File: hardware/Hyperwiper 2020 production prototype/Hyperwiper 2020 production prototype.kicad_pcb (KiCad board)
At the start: 2 copper layers, 79.5 x 57.3 mm, 20 parts, among them J1 Conn_01x05, K1 Main Power relay, K2 Wiper control relay, Q1 PN2222A, SW1 ON-OFF, SW2 SW_Reed, U1 Teensy4.0, U3 L7805

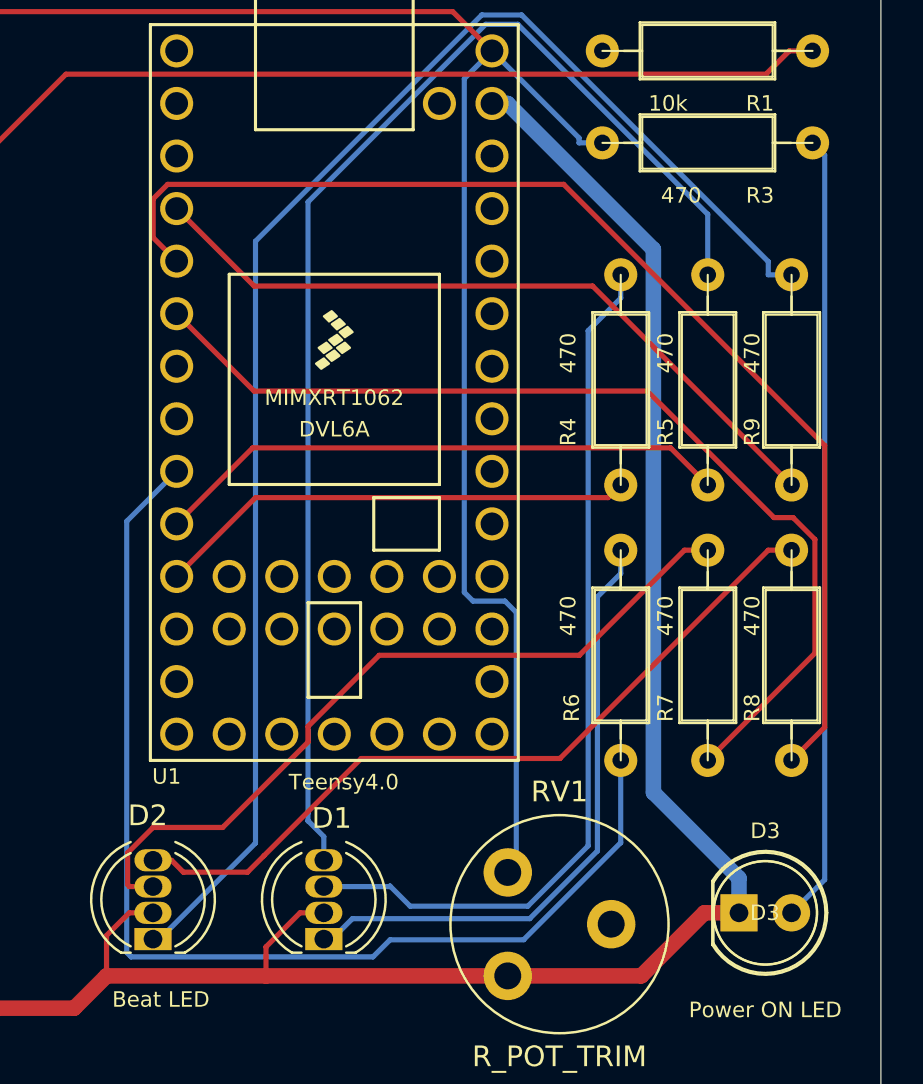
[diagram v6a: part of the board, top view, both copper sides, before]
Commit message: Added flowchart drafts and modified pin number after finding conflics with the audio board I2C bus
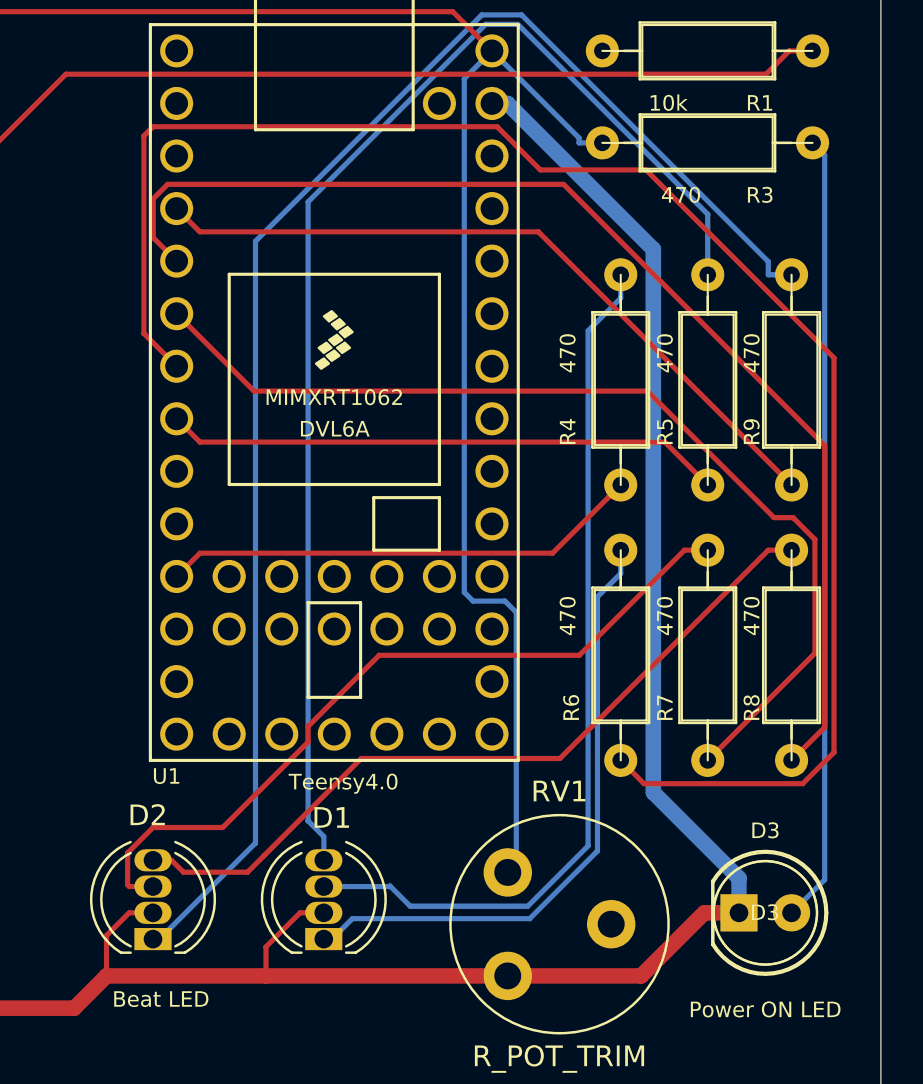
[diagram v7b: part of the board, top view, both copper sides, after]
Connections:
- U1 pad 10: /M_LED_g -> Net-(U1-Pad10)
- U1 pad 7: Net-(U1-Pad7) -> /M_LED_r
- U1 pad 8: Net-(U1-Pad8) -> /M_LED_g
- U1 pad 9: /M_LED_r -> Net-(U1-Pad9)
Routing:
- net /M_LED_r: track 54.5 -> 80.4 mm
- net /M_LED_g: track 27.9 -> 27.0 mm
- net /M_LED_b: track 23.3 -> 24.2 mm
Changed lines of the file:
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@@
   (net 26 "Net-(U1-Pad2)")
   (net 27 "Net-(U1-Pad3)")
-  (net 28 "Net-(U1-Pad7)")
-  (net 29 "Net-(U1-Pad8)")
+  (net 28 "Net-(U1-Pad9)")
+  (net 29 "Net-(U1-Pad10)")
   (net 30 "Net-(U1-Pad12)")
   (net 31 "Net-(U1-Pad13)")
@@
       (net 21 "/B_LED_b") (pinfunction "4_BCLK2"))
     (pad "7" thru_hole circle (at -1.27 7.62 270) (size 1.6 1.6) (drill 1.1) (layers *.Cu *.Mask)
-      (net 28 "Net-(U1-Pad7)") (pinfunction "5_IN2"))
+      (net 20 "/M_LED_r") (pinfunction "5_IN2"))
     (pad "8" thru_hole circle (at 1.27 7.62 270) (size 1.6 1.6) (drill 1.1) (layers *.Cu *.Mask)
-      (net 29 "Net-(U1-Pad8)") (pinfunction "6_OUT1D"))
+      (net 19 "/M_LED_g") (pinfunction "6_OUT1D"))
     (pad "9" thru_hole circle (at 3.81 7.62 270) (size 1.6 1.6) (drill 1.1) (layers *.Cu *.Mask)
-      (net 20 "/M_LED_r") (pinfunction "7_RX2_OUT1A"))
+      (net 28 "Net-(U1-Pad9)") (pinfunction "7_RX2_OUT1A"))
     (pad "10" thru_hole circle (at 6.35 7.62 270) (size 1.6 1.6) (drill 1.1) (layers *.Cu *.Mask)
-      (net 19 "/M_LED_g") (pinfunction "8_TX2_IN1"))
+      (net 29 "Net-(U1-Pad10)") (pinfunction "8_TX2_IN1"))
     (pad "11" thru_hole circle (at 8.89 7.62 270) (size 1.6 1.6) (drill 1.1) (layers *.Cu *.Mask)
       (net 18 "/M_LED_b") (pinfunction "9_OUT1C"))
@@
   (segment (start 104.612 82.387) (end 114.52 82.387) (width 0.25) (layer "F.Cu") (net 15))
   (segment (start 114.52 82.387) (end 117.523 79.3845) (width 0.25) (layer "F.Cu") (net 15))
-  (segment (start 144.068 86.0695) (end 147.878 82.2595) (width 0.25) (layer "F.Cu") (net 18))
-  (segment (start 147.878 82.2595) (end 164.921 82.2595) (width 0.25) (layer "F.Cu") (net 18))
+  (segment (start 144.068 86.0695) (end 145.193001 84.944499) (width 0.25) (layer "F.Cu") (net 18))
   (segment (start 164.921 82.2595) (end 165.531 81.6495) (width 0.25) (layer "F.Cu") (net 18))
-  (segment (start 147.7423 79.8552) (end 167.9417 79.8552) (width 0.25) (layer "F.Cu") (net 19))
-  (segment (start 144.068 83.5295) (end 147.7423 79.8552) (width 0.25) (layer "F.Cu") (net 19))
-  (segment (start 167.9417 79.8552) (end 169.736 81.6495) (width 0.25) (layer "F.Cu") (net 19))
-  (segment (start 141.6554 83.4021) (end 141.6554 104.2435) (width 0.25) (layer "B.Cu") (net 20))
-  (segment (start 144.068 80.9895) (end 141.6554 83.4021) (width 0.25) (layer "B.Cu") (net 20))
-  (segment (start 141.8683 104.4564) (end 153.5559 104.4564) (width 0.25) (layer "B.Cu") (net 20))
-  (segment (start 160.8393 103.6278) (end 165.531 98.9361) (width 0.25) (layer "B.Cu") (net 20))
-  (segment (start 141.6554 104.2435) (end 141.8683 104.4564) (width 0.25) (layer "B.Cu") (net 20))
-  (segment (start 154.3845 103.6278) (end 160.8393 103.6278) (width 0.25) (layer "B.Cu") (net 20))
-  (segment (start 165.531 98.9361) (end 165.531 94.9595) (width 0.25) (layer "B.Cu") (net 20))
-  (segment (start 153.5559 104.4564) (end 154.3845 103.6278) (width 0.25) (layer "B.Cu") (net 20))
+  (segment (start 145.193001 84.944499) (end 162.236001 84.944499) (width 0.25) (layer "F.Cu") (net 18))
+  (segment (start 162.236001 84.944499) (end 165.531 81.6495) (width 0.25) (layer "F.Cu") (net 18))
+  (segment (start 169.736 81.6495) (end 167.661001 79.574501) (width 0.25) (layer "F.Cu") (net 19))
+  (segment (start 145.193001 79.574501) (end 144.068 78.4495) (width 0.25) (layer "F.Cu") (net 19))
+  (segment (start 167.661001 79.574501) (end 145.193001 79.574501) (width 0.25) (layer "F.Cu") (net 19))
+  (segment (start 142.48519 74.32669) (end 144.068 75.9095) (width 0.25) (layer "F.Cu") (net 20))
+  (segment (start 142.929499 64.334501) (end 142.48519 64.77881) (width 0.25) (layer "F.Cu") (net 20))
+  (segment (start 175.838009 94.572493) (end 175.838009 75.508009) (width 0.25) (layer "F.Cu") (net 20))
+  (segment (start 142.48519 64.77881) (end 142.48519 74.32669) (width 0.25) (layer "F.Cu") (net 20))
+  (segment (start 161.644502 66.421) (end 159.558003 64.334501) (width 0.25) (layer "F.Cu") (net 20))
+  (segment (start 159.558003 64.334501) (end 142.929499 64.334501) (width 0.25) (layer "F.Cu") (net 20))
+  (segment (start 166.656001 96.084501) (end 174.326001 96.084501) (width 0.25) (layer "F.Cu") (net 20))
+  (segment (start 166.751 66.421) (end 161.644502 66.421) (width 0.25) (layer "F.Cu") (net 20))
+  (segment (start 175.838009 75.508009) (end 166.751 66.421) (width 0.25) (layer "F.Cu") (net 20))
+  (segment (start 174.326001 96.084501) (end 175.838009 94.572493) (width 0.25) (layer "F.Cu") (net 20))
+  (segment (start 165.531 94.9595) (end 166.656001 96.084501) (width 0.25) (layer "F.Cu") (net 20))
   (segment (start 166.8207 77.1091) (end 172.9361 83.2245) (width 0.25) (layer "F.Cu") (net 21))
   (segment (start 172.9361 83.2245) (end 173.8577 83.2245) (width 0.25) (layer "F.Cu") (net 21))
@@
   (segment (start 143.6315 67.119) (end 162.7718 67.119) (width 0.25) (layer "F.Cu") (net 22))
   (segment (start 142.9352 67.8153) (end 143.6315 67.119) (width 0.25) (layer "F.Cu") (net 22))
-  (segment (start 164.1701 72.0336) (end 173.786 81.6495) (width 0.25) (layer "F.Cu") (net 23))
-  (segment (start 144.068 68.2895) (end 147.8121 72.0336) (width 0.25) (layer "F.Cu") (net 23))
-  (segment (start 147.8121 72.0336) (end 164.1701 72.0336) (width 0.25) (layer "F.Cu") (net 23))
+  (segment (start 161.551001 69.414501) (end 173.786 81.6495) (width 0.25) (layer "F.Cu") (net 23))
+  (segment (start 145.193001 69.414501) (end 161.551001 69.414501) (width 0.25) (layer "F.Cu") (net 23))
+  (segment (start 144.068 68.2895) (end 145.193001 69.414501) (width 0.25) (layer "F.Cu") (net 23))
   (segment (start 151.18 103.596) (end 151.575 103.596) (width 0.25) (layer "B.Cu") (net 61))
   (segment (start 151.575 103.596) (end 152.562 102.608) (width 0.25) (layer "B.Cu") (net 61))

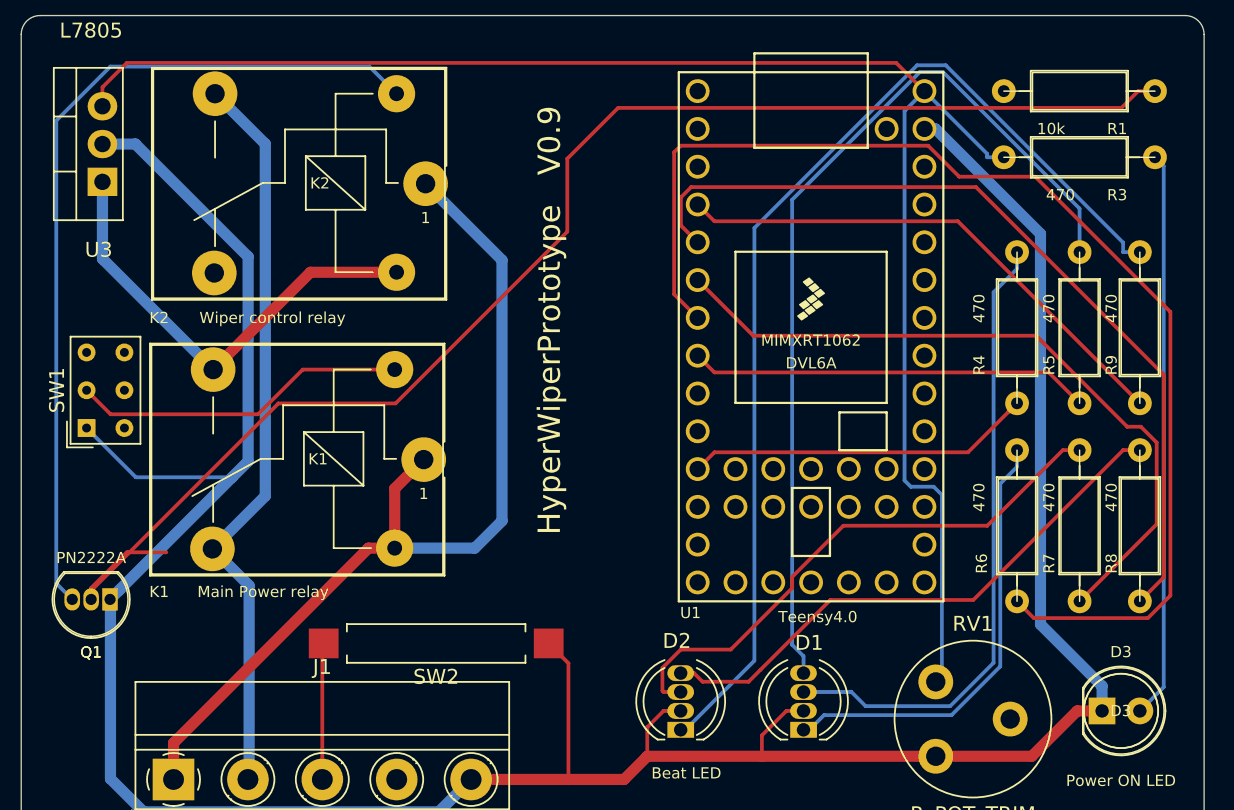
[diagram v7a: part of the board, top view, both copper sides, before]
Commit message: Assined pins and updated firmware
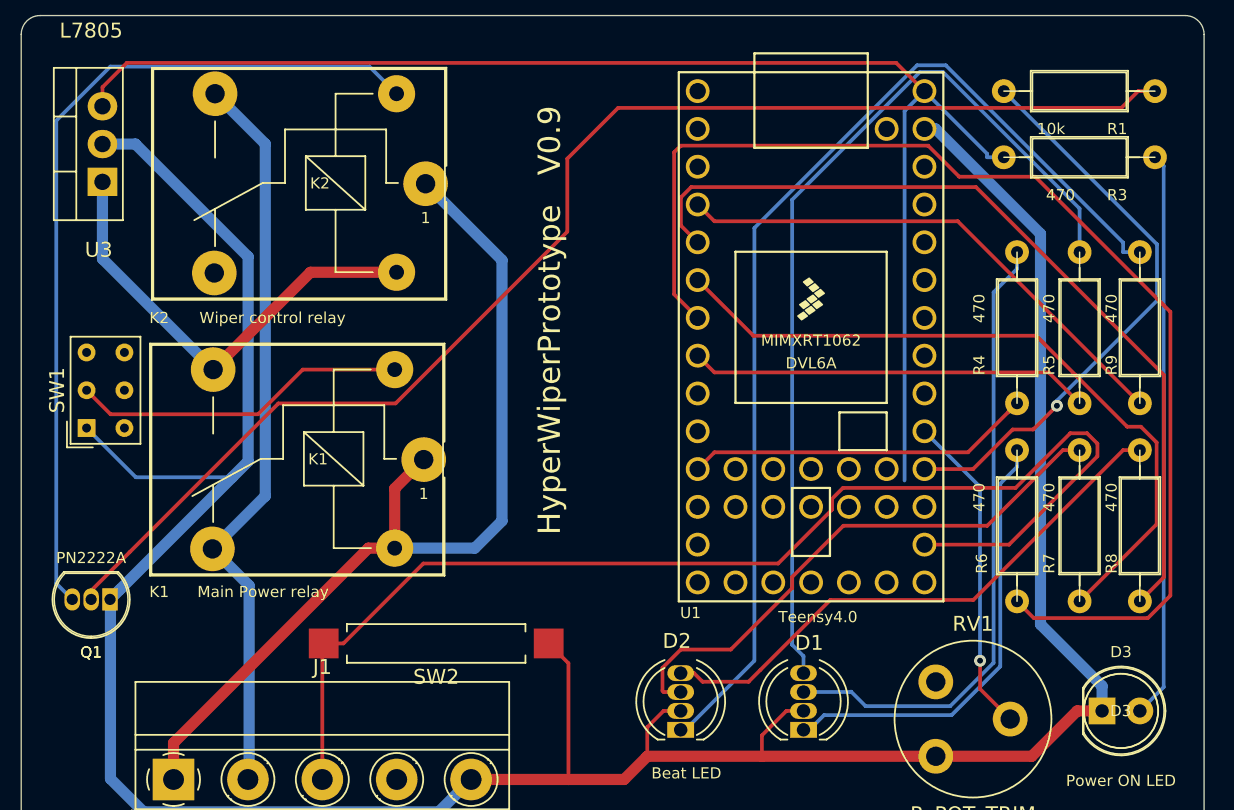
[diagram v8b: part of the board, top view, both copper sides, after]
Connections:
- U1 pad 21: Net-(U1-Pad21) -> /reed
- U1 pad 23: Net-(U1-Pad23) -> /motor_start
- U1 pad 24: Net-(U1-Pad24) -> /Pot
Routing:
- net /reed: track 9.18 -> 82.7 mm
- net /motor_start: track 0.00 -> 38.9 mm, vias 0 -> 1
- net /Pot: track 0.00 -> 21.7 mm, vias 0 -> 1
- net /5V: track 107.7 -> 92.0 mm
- net Net-(Q1-Pad2): track 95.7 -> 88.3 mm
